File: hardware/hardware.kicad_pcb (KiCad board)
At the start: 2 copper layers, 81 x 60.5 mm, 213 parts, among them J1 USB_B_Micro, J2 RJ45_Hanrun_HR911105A_Horizon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, J3 Conn_02x05_Odd_Even, J4 Conn_02x03_Odd_Even, J5 Conn_01x02, U10 CH32V003F4P6, U11 CH32V003F4P6, U12 CH32V003F4P6, U13 CH32V003F4P6, U14 CH32V003F4P6, U15 CH32V003F4P6, U16 CH32V003F4P6, U17 CH32V003F4P6, U18 CH32V003F4P6, U19 CH32V003F4P6, U2 CH32V003F4P6, U20 CH32V003F4P6, U21 CH32V003F4P6, U22 CH32V003F4P6, U23 CH32V003F4P6, U24 CH32V003F4P6, U25 CH32V003F4P6, U26 CH32V003F4P6, U27 CH32V003F4P6, U28 CH32V307RCT6, U3 AMS1117-3.3, U4 CH340C, U5 CH32V003F4P6, U6 CH32V003F4P6, U7 CH32V003F4P6, U8 CH32V003F4P6, U9 CH32V003F4P6, Y1 Crystal_GND24

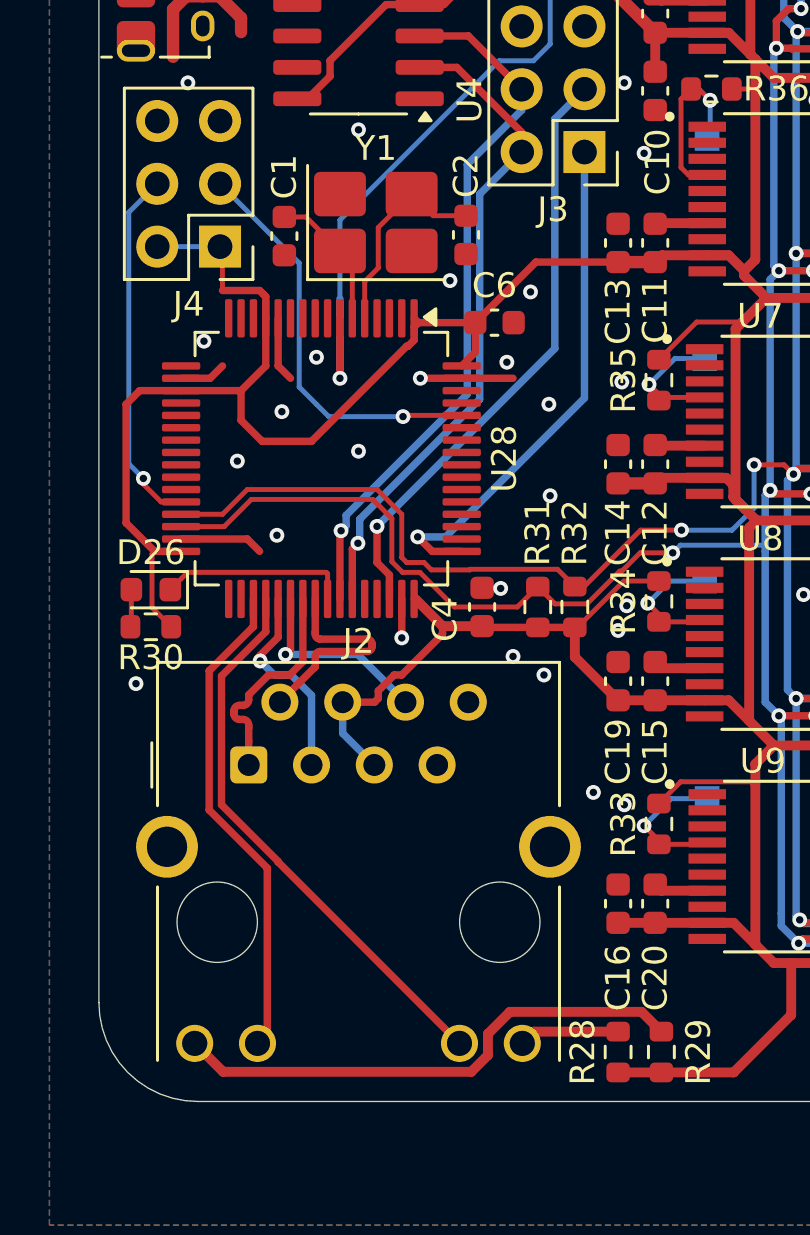
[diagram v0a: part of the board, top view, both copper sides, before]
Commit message: update ehernet wiring
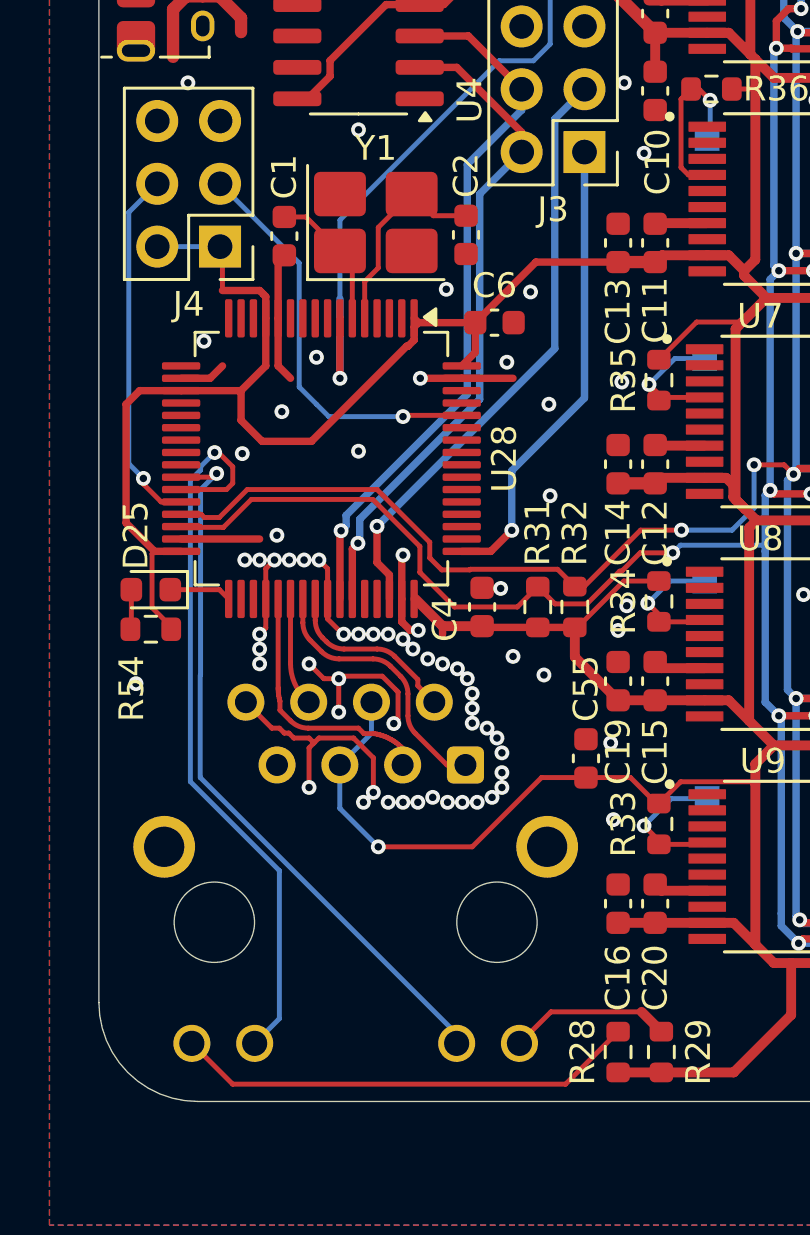
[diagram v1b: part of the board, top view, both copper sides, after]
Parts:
- removed D26: LED, LED_SMD:LED_0603_1608Metric
- removed R30: R_Small, Resistor_SMD:R_0603_1608Metric
- added C55: 10pf, Capacitor_SMD:C_0603_1608Metric, F.Cu at (55.2, 89.6)
- added D25: LED, LED_SMD:LED_0603_1608Metric, F.Cu at (37.6, 82.8)
- added R54: R_Small, Resistor_SMD:R_0603_1608Metric, F.Cu at (37.6, 84.4)
- J2: moved to B.Cu
- moved J2 8.77 mm to (50.3, 89.9), turned to 180 degrees
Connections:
- U28 pad 26: unconnected-(U28-ADC8/PB0-Pad26) -> LED2
- U28 pad 27: unconnected-(U28-ADC9/PB1-Pad27) -> LED1
- U28 pad 33: unconnected-(U28-PB12-Pad33) -> Net-(D25-K)
- U28 pad 35: LED2 -> unconnected-(U28-PB14-Pad35)
- U28 pad 36: LED1 -> GND
- U28 pad 41: Net-(D26-K) -> GND
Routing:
- net GND: track 69.8 -> 97.3 mm, vias 72 -> 115
- net Net-(J2-Pad12): track 4.07 -> 18.8 mm
- net Net-(J2-Pad9): track 21.2 -> 6.60 mm
- net +3V3: track 749.1 -> 760.6 mm, vias 0 -> 1
- net LED2: track 19.9 -> 29.1 mm, vias 0 -> 1
- net Net-(D26-K): track 7.70 -> 0.00 mm
- net LED1: track 22.7 -> 30.0 mm, vias 0 -> 1
- net RDN: track 7.98 -> 4.38 mm, vias 1 -> 0
- net Net-(D25-K): track 0.00 -> 2.52 mm
- net RDP: track 8.28 -> 10.7 mm, vias 1 -> 0
- net SWCLK: track 21.0 -> 18.9 mm
- net TDP: track 8.89 -> 10.9 mm
- net TDN: track 8.99 -> 7.29 mm
- net Net-(D26-A): track 1.52 -> 0.00 mm
- net Net-(D25-A): track 0.00 -> 1.52 mm
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
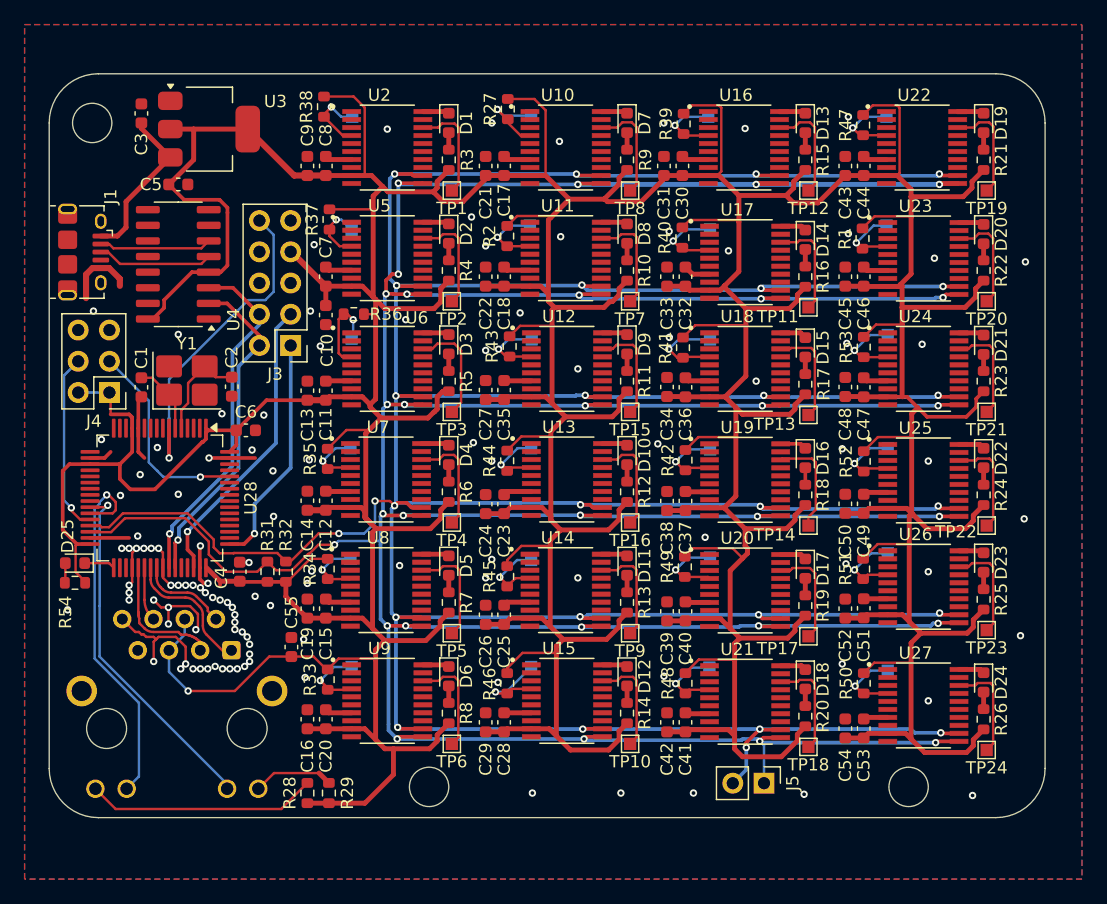
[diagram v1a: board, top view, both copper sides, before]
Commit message: pass to 4 layers pcb
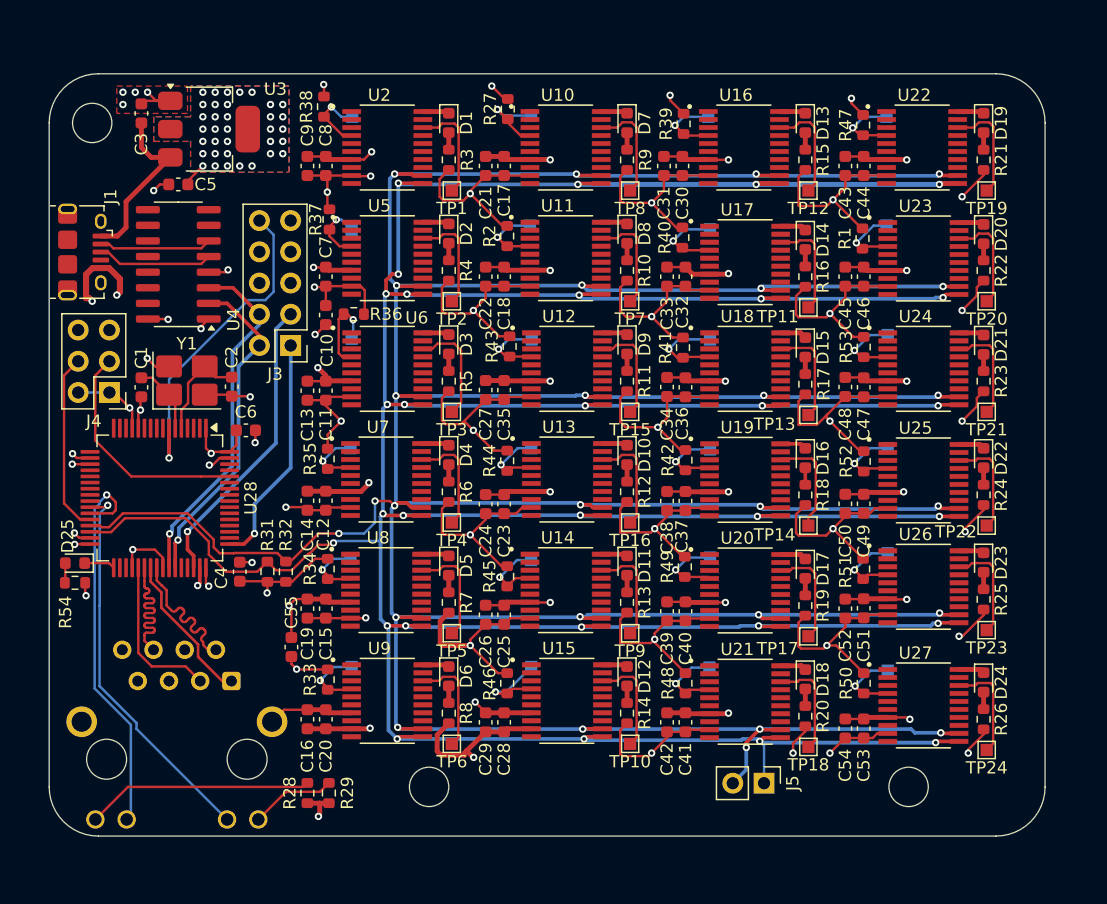
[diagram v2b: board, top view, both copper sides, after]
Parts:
- moved J2 2.50 mm to (50.3, 92.4)
- turned C5 to 180 degrees
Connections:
- net RDN renamed RD_N
- net RDP renamed RD_P
- net TDN renamed TD_N
- net TDP renamed TD_P
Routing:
- net +3V3: track 760.6 -> 361.2 mm, vias 1 -> 82
- net GND: track 97.3 -> 166.6 mm, vias 115 -> 42
- net RD_N: track 4.38 -> 12.8 mm
- net TD_N: track 7.29 -> 12.3 mm
- net LED2: track 29.1 -> 31.6 mm
- net BOOT0: track 16.7 -> 19.1 mm, vias 1 -> 0
- net RD_P: track 10.7 -> 12.9 mm
- net LED1: track 30.0 -> 32.0 mm
- net TD_P: track 10.9 -> 12.4 mm
- net +5V: track 13.3 -> 14.2 mm
- net BOOT1: vias 1 -> 0
- added copper zone on B.Cu, net +3V3
- added copper zone on F.Cu, net +3V3
- added copper zone on In2.Cu, net +3V3
- added copper zone on In1.Cu, net GND
- removed copper zone on B.Cu, net GND
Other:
- board size 81 x 60.5 mm -> 81 x 62 mm
- copper layers 2 -> 4

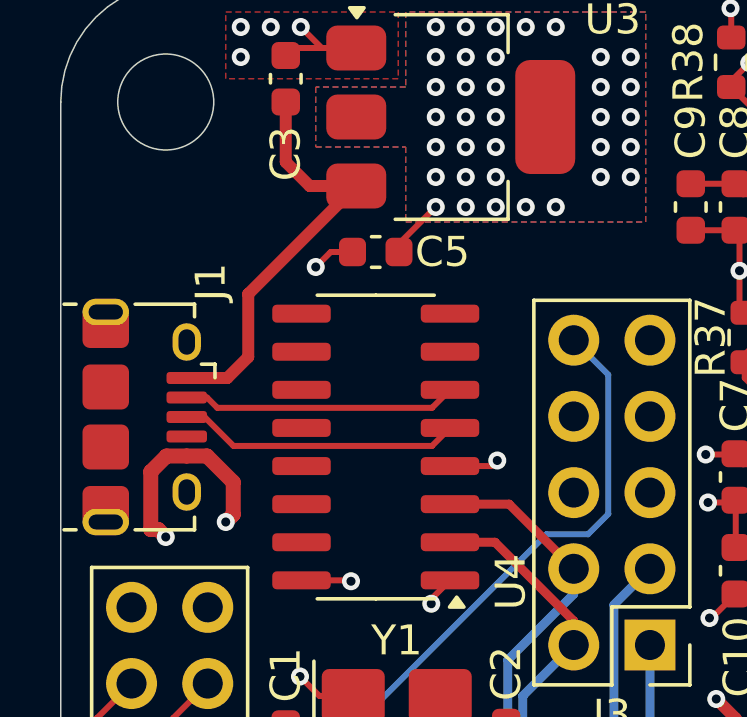
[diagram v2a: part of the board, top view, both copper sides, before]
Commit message: add ethernet
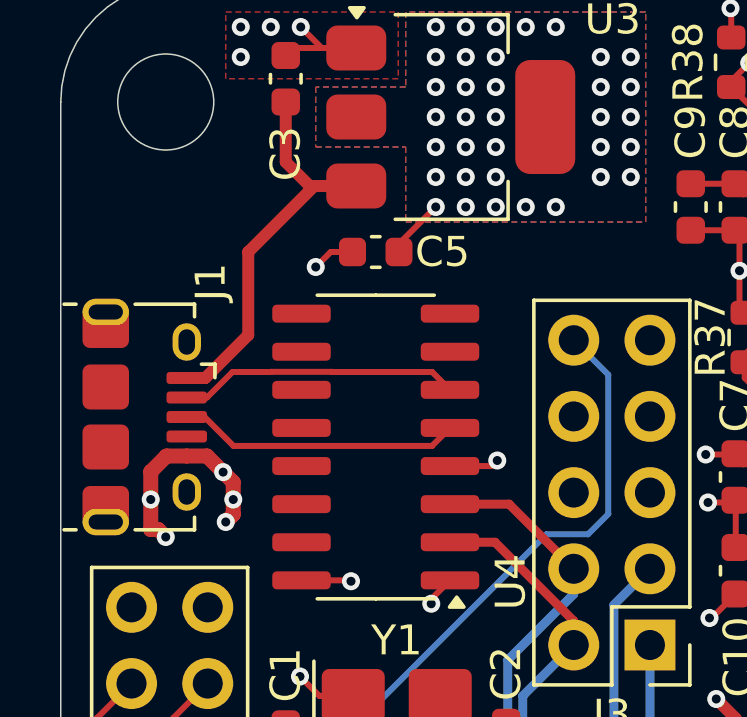
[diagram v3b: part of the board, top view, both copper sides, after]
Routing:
- net GND: vias 42 -> 45
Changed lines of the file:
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@@
 	)
 	(segment
-		(start 41.75 55.5)
-		(end 41.75 53.4)
+		(start 43 47)
+		(end 43 49)
 		(width 0.4)
 		(layer "F.Cu")
@@
 	)
 	(segment
-		(start 43 47)
-		(end 43 49)
+		(start 43 49)
+		(end 43.8 49.8)
 		(width 0.4)
 		(layer "F.Cu")
@@
 	)
 	(segment
-		(start 43 49)
-		(end 43.8 49.8)
+		(start 41.75 54.767892)
+		(end 41.75 52)
 		(width 0.4)
 		(layer "F.Cu")
@@
 	)
 	(segment
-		(start 39.7 56.2)
-		(end 41.05 56.2)
+		(start 43.95 49.8)
+		(end 45.35 49.8)
 		(width 0.4)
 		(layer "F.Cu")
@@
 	)
 	(segment
-		(start 41.05 56.2)
-		(end 41.75 55.5)
+		(start 40.317892 56.2)
+		(end 41.75 54.767892)
 		(width 0.4)
 		(layer "F.Cu")
@@
 	)
 	(segment
-		(start 41.75 53.4)
-		(end 45.35 49.8)
+		(start 41.75 52)
+		(end 43.95 49.8)
+		(width 0.4)
+		(layer "F.Cu")
+		(net 1)
+	)
+	(segment
+		(start 39.7 56.2)
+		(end 40.317892 56.2)
 		(width 0.4)
 		(layer "F.Cu")
@@
 	(segment
 		(start 41.25 59.675001)
-		(end 41.25 60.75)
+		(end 41.25 60.25)
+		(width 0.5)
+		(layer "F.Cu")
+		(net 2)
+	)
+	(segment
+		(start 40.912499 59.337501)
+		(end 41.25 59.675001)
 		(width 0.5)
 		(layer "F.Cu")
@@
 	)
 	(segment
+		(start 41.25 60.25)
+		(end 41.25 60.75)
+		(width 0.5)
+		(layer "F.Cu")
+		(net 2)
+	)
+	(segment
 		(start 74.71 94.975)
 		(end 72.5 94.975)
@@
 	(segment
 		(start 40.374999 58.8)
-		(end 41.25 59.675001)
+		(end 40.912499 59.337501)
 		(width 0.5)
 		(layer "F.Cu")
@@
 	)
 	(segment
+		(start 38.5 60.25)
+		(end 38.5 61.25)
+		(width 0.5)
+		(layer "F.Cu")
+		(net 2)
+	)
+	(segment
 		(start 102 49.975)
 		(end 101.75 49.725)
@@
 	(segment
 		(start 38.5 59.325001)
-		(end 38.5 61.25)
+		(end 38.5 60.25)
 		(width 0.5)
 		(layer "F.Cu")
@@
 	)
 	(via
+		(at 40.912499 59.337501)
+		(size 0.6)
+		(drill 0.3)
+		(layers "F.Cu" "B.Cu")
+		(net 2)
+	)
+	(via
 		(at 76.25 50)
 		(size 0.6)
@@
 	)
 	(via
+		(at 38.5 60.25)
+		(size 0.6)
+		(drill 0.3)
+		(layers "F.Cu" "B.Cu")
+		(net 2)
+	)
+	(via
 		(at 105.5 95.5)
 		(size 0.6)
@@
 	)
 	(via
+		(at 41.25 60.25)
+		(size 0.6)
+		(drill 0.3)
+		(layers "F.Cu" "B.Cu")
+		(net 2)
+	)
+	(via
 		(at 52.25 73)
 		(size 0.6)
@@
 	)
 	(segment
-		(start 47.875 57.195)
-		(end 40.719999 57.195)
+		(start 42.509032 55.994)
+		(end 44.540968 55.994)
 		(width 0.2)
 		(layer "F.Cu")
@@
 	)
 	(segment
-		(start 40.374999 56.85)
-		(end 39.7 56.85)
+		(start 39.7 56.85)
+		(end 40.374999 56.85)
 		(width 0.2)
 		(layer "F.Cu")
@@
 	)
 	(segment
-		(start 40.719999 57.195)
-		(end 40.374999 56.85)
+		(start 42.503032 56)
+		(end 42.509032 55.994)
 		(width 0.2)
 		(layer "F.Cu")
@@
 	)
 	(segment
-		(start 48.475 56.595)
-		(end 47.875 57.195)
+		(start 44.546968 56)
+		(end 47.88 56)
 		(width 0.2)
 		(layer "F.Cu")
@@
 	)
 	(segment
-		(start 40.293456 57.5)
-		(end 39.7 57.5)
+		(start 44.540968 55.994)
+		(end 44.546968 56)
 		(width 0.2)
 		(layer "F.Cu")
-		(net 7)
+		(net 6)
 	)
 	(segment
-		(start 41.258456 58.465)
-		(end 40.293456 57.5)
+		(start 40.374999 56.85)
+		(end 41.224999 56)
 		(width 0.2)
 		(layer "F.Cu")
-		(net 7)
+		(net 6)
+	)
+	(segment
+		(start 47.88 56)
+		(end 48.475 56.595)
+		(width 0.2)
+		(layer "F.Cu")
+		(net 6)
+	)
+	(segment
+		(start 41.224999 56)
+		(end 42.503032 56)
+		(width 0.2)
+		(layer "F.Cu")
+		(net 6)
 	)
 	(segment
@@
 		(width 0.2)
 		(layer "F.Cu")
+		(net 7)
+	)
+	(segment
+		(start 40.293456 57.5)
+		(end 39.7 57.5)
+		(width 0.2)
+		(layer "F.Cu")
+		(net 7)
+	)
+	(segment
+		(start 41.258456 58.465)
+		(end 40.293456 57.5)
+		(width 0.2)
+		(layer "F.Cu")
